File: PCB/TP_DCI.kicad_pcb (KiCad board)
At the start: 2 copper layers, 85.7 x 178.9 mm, 70 parts, among them J8 Molex_KK254, J9 Molex_KK254, K1 G5V-1, K2 G5V-1, P1 Conn_Poncho2P_2x_20x2, Q1 BC817W, Q2 BC817W, U1 PS2805-4, U2 ACS725xLCTR-10AU, U4 ACS725xLCTR-10AU, U5 24AA1025, U6 DS3231

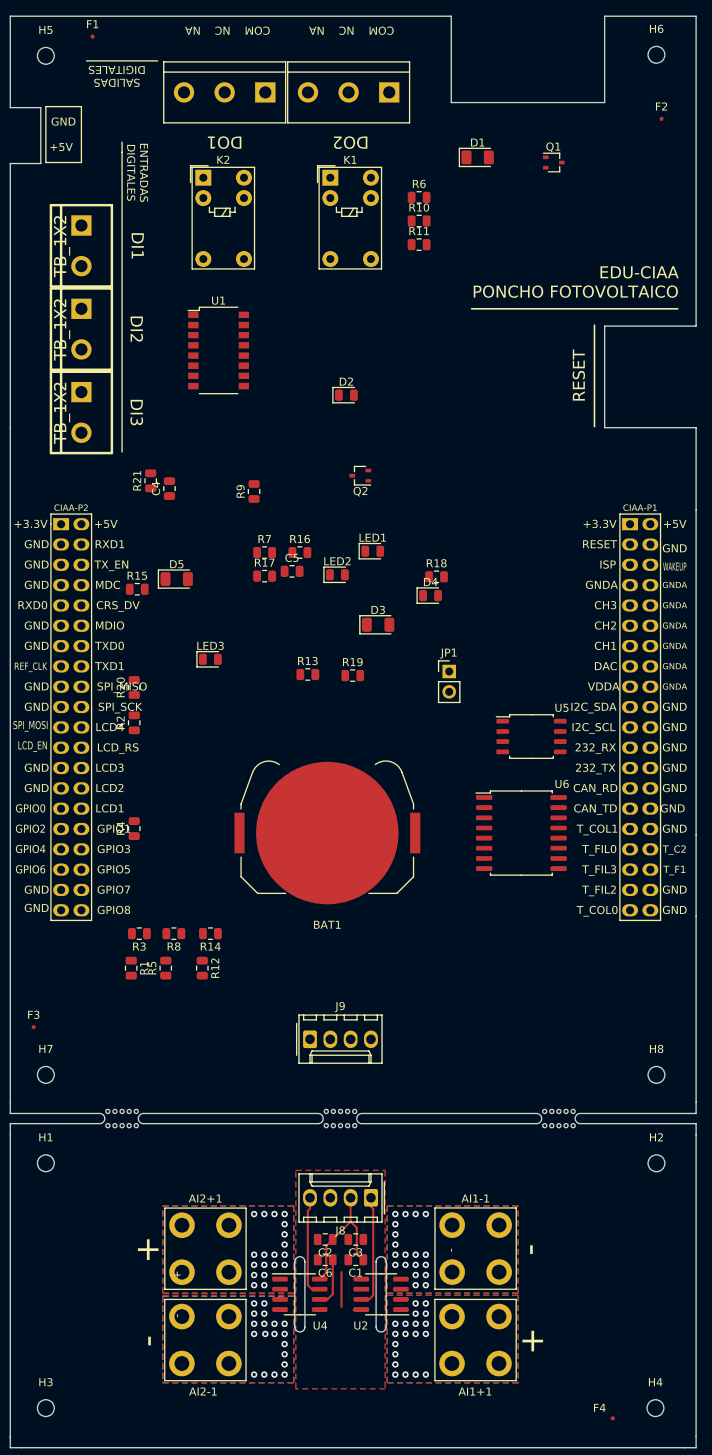
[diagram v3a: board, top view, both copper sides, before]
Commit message: actualizaciones de esquematico segun correcciones del docente
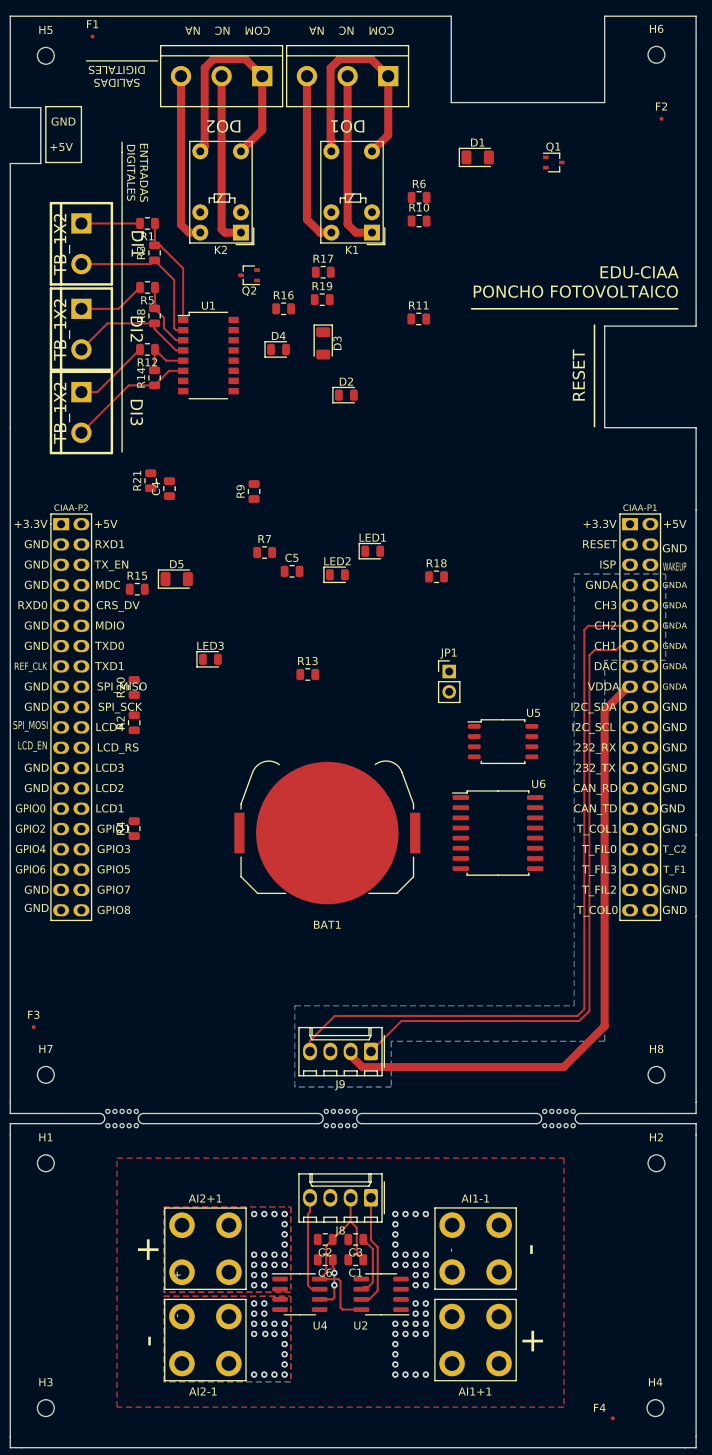
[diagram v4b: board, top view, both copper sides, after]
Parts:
- H1, H2, H3, H4: value Hole -> MountingHole
- moved R1 93.1 mm to (36.8, 43.8), turned to 180 degrees
- moved R5 85.1 mm to (36.8, 51.8), turned to 180 degrees
- moved R3 85.1 mm to (37.7, 47.5), turned to 90 degrees
- moved R12 77.6 mm to (36.8, 59.6), turned to 180 degrees
- moved R8 77.3 mm to (37.7, 55.4), turned to 90 degrees
- moved R14 69.8 mm to (37.7, 63.1), turned to 90 degrees
- moved R19 47.1 mm to (58.7, 53.3)
- moved R17 38.7 mm to (58.8, 49.9)
- moved D4 36.2 mm to (53.2, 59.6)
- moved D3 35.8 mm to (58.8, 58.8), turned to 270 degrees
- moved R16 30.5 mm to (53.8, 54.5)
- moved Q2 28.7 mm to (49.5, 50.3)
- moved DO2 16.0 mm to (46.1, 25.4)
- moved DO1 15.5 mm to (61.8, 25.4)
- moved R11 9.29 mm to (70.7, 55.8)
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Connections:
- P1 pad 10: (no net) -> GNDA
- P1 pad 7: (no net) -> GNDA
- P1 pad 8: (no net) -> GNDA
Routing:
- net /ADC_CH2: track 0.00 -> 90.6 mm
- net /ADC_CH1: track 0.00 -> 79.4 mm
- net VDDA: track 0.00 -> 78.8 mm
- net /COM2: track 0.00 -> 29.7 mm
- net /COM1: track 0.00 -> 29.2 mm
- net /NC1: track 0.00 -> 22.0 mm
- net /NC2: track 0.00 -> 21.7 mm
- net /NA1: track 0.00 -> 21.6 mm
- net /NA2: track 0.00 -> 21.4 mm
- net Net-(DI1-Pad2): track 0.00 -> 20.1 mm
- net Net-(DI2-Pad2): track 0.00 -> 16.1 mm
- net Net-(DI3-Pad2): track 0.00 -> 15.9 mm
- net Net-(R1-Pad1): track 0.00 -> 14.0 mm
- net Net-(DI3-Pad1): track 0.00 -> 9.53 mm
- net Net-(R5-Pad1): track 0.00 -> 8.63 mm
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- added copper zone on B.Cu, net GNDA
- removed copper zone on B.Cu, net Net-(AI1+1-Pad1)
- removed copper zone on F.Cu, net Net-(AI1+1-Pad1)
- removed copper zone on B.Cu, net Net-(AI1-1-Pad1)
- removed copper zone on F.Cu, net Net-(AI1-1-Pad1)
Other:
- outline, holes or cut-outs redrawn
- net class Default: clearance 0.2 -> 0.35
- rule trace_clearance: 0.2 -> 0.35

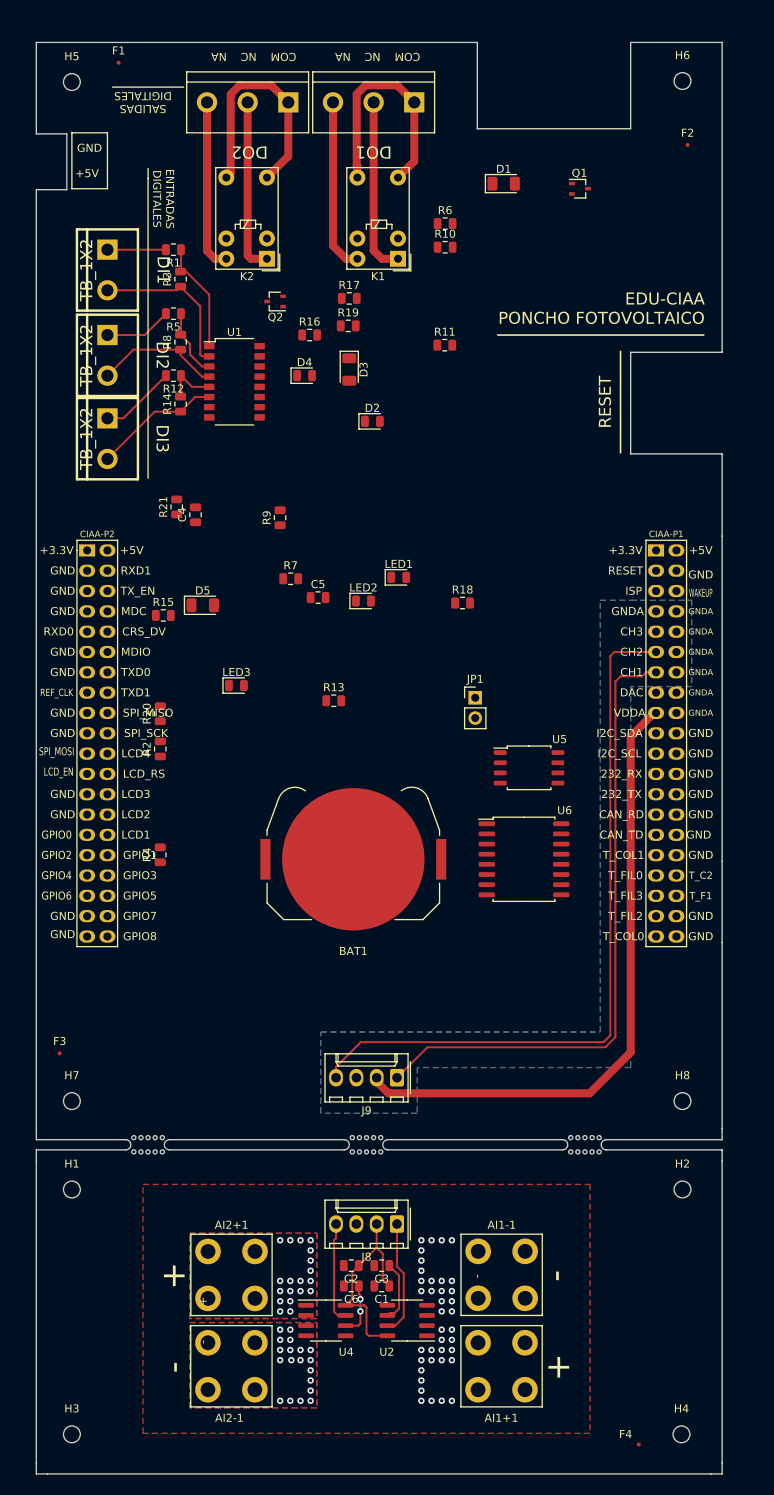
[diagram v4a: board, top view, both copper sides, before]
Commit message: avances en ruteo del PCB
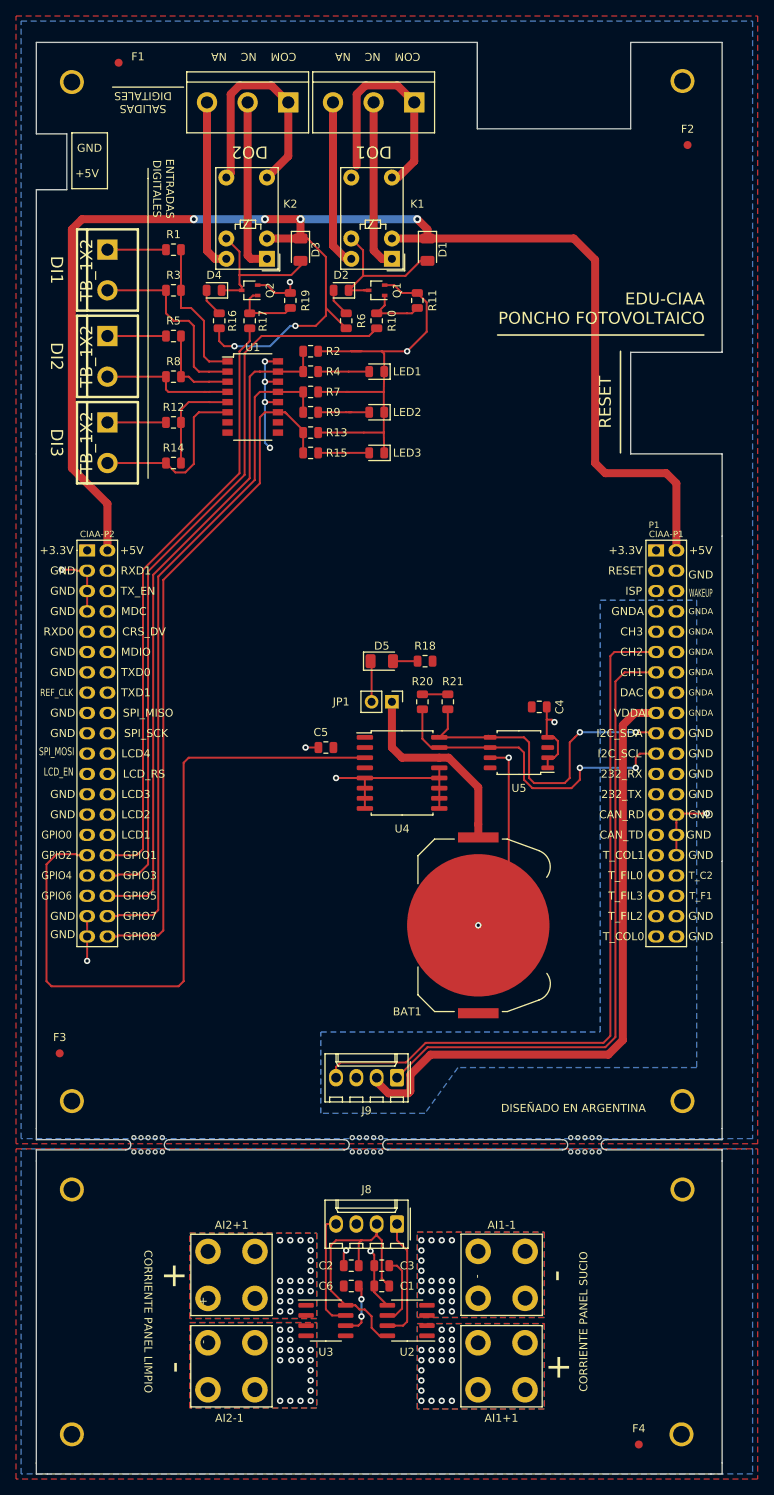
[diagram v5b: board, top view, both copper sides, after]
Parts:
- F1, F2, F3, F4: footprint Fiducial:Fiducial_0.5mm_Mask1mm -> Fiducial:Fiducial_1mm_Mask2mm
- moved R4 63.3 mm to (54.0, 59.1), turned to 0 degrees
- moved R2 53.2 mm to (54.0, 56.5), turned to 0 degrees
- moved C4 49.2 mm to (82.5, 101.0), turned to 0 degrees
- moved R21 41.7 mm to (71.1, 100.3), turned to 270 degrees
- moved LED3 34.0 mm to (62.2, 69.2), turned to 180 degrees
- moved R13 33.6 mm to (54.0, 66.7)
- moved R20 32.8 mm to (67.9, 100.3), turned to 270 degrees
- moved Q1 28.4 mm to (62.2, 48.9), turned to 180 degrees
- moved R15 27.4 mm to (54.0, 69.2)
- moved LED1 25.9 mm to (62.2, 59.1), turned to 180 degrees
- moved LED2 23.7 mm to (62.2, 64.1), turned to 180 degrees
- moved R7 23.5 mm to (54.0, 61.6)
- moved D5 23.4 mm to (62.9, 95.2)
- moved C5 18.8 mm to (55.9, 106.0), turned to 180 degrees
- moved U4 18.7 mm to (65.4, 109.2)
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- renumbered U4 to U3, U6 to U4
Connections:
- C4 pad 1: /+3.3V -> +3V3
- C5 pad 1: /+3.3V -> +3V3
- P1 pad 72: /GPIO1 -> Net-(P1-Pad72)
- P1 pad 74: /GPIO3 -> Net-(P1-Pad74)
- P1 pad 76: /GPIO5 -> Net-(P1-Pad76)
- P1 pad 78: /GPIO7 -> Net-(P1-Pad78)
- P1 pad 80: /GPIO8 -> Net-(P1-Pad80)
- R10 pad 2: /GPIO7 -> Net-(P1-Pad74)
- R13 pad 1: /GPIO5 -> Net-(P1-Pad80)
- R14 pad 1: Net-(DI3-Pad2) -> Net-(R12-Pad1)
- R14 pad 2: Net-(R12-Pad1) -> Net-(DI3-Pad2)
- R15 pad 1: /GPIO5 -> Net-(P1-Pad80)
- R17 pad 2: /GPIO8 -> Net-(P1-Pad72)
- R2 pad 1: /GPIO1 -> Net-(P1-Pad76)
- R3 pad 1: Net-(DI1-Pad2) -> Net-(R1-Pad1)
- R3 pad 2: Net-(R1-Pad1) -> Net-(DI1-Pad2)
- R4 pad 1: /GPIO1 -> Net-(P1-Pad76)
- R7 pad 1: /GPIO3 -> Net-(P1-Pad78)
- R8 pad 1: Net-(DI2-Pad2) -> Net-(R5-Pad1)
- R8 pad 2: Net-(R5-Pad1) -> Net-(DI2-Pad2)
- R9 pad 1: /GPIO3 -> Net-(P1-Pad78)
- U1 pad 11: /GPIO5 -> Net-(P1-Pad80)
- U1 pad 13: /GPIO3 -> Net-(P1-Pad78)
- U1 pad 15: /GPIO1 -> Net-(P1-Pad76)
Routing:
- net +5V: track 0.00 -> 198.6 mm, vias 0 -> 6
- net GND: track 0.00 -> 142.9 mm, vias 0 -> 10
- net Net-(P1-Pad74): track 0.00 -> 92.4 mm
- net /GPIO2: track 0.00 -> 88.2 mm
- net Net-(P1-Pad80): track 0.00 -> 86.2 mm
- net Net-(P1-Pad76): track 0.00 -> 84.8 mm
- net Net-(P1-Pad78): track 0.00 -> 84.7 mm
- net Net-(P1-Pad72): track 0.00 -> 75.4 mm
- net /SDA: track 0.00 -> 41.9 mm, vias 0 -> 2
- net /SCL: track 0.00 -> 40.8 mm, vias 0 -> 2
- net Net-(BAT1-Pad1): track 0.00 -> 24.8 mm
- net Net-(D1-Pad2): track 0.00 -> 19.8 mm
- net +3V3: track 0.00 -> 19.7 mm, vias 0 -> 4
- net Net-(D3-Pad2): track 0.00 -> 18.5 mm
- net Net-(C1-Pad2): track 0.00 -> 9.69 mm, vias 0 -> 2
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- added copper zone on F.Cu, net +3V3
- added copper zone on B.Cu, net GND
- added copper zone on B.Cu, net Net-(AI1+1-Pad1)
- added copper zone on F.Cu, net Net-(AI1+1-Pad1)
- added copper zone on B.Cu, net Net-(AI1-1-Pad1)
- added copper zone on F.Cu, net Net-(AI1-1-Pad1)
- added copper zone on B.Cu, net Net-(C1-Pad2)
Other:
- net class Default: clearance 0.35 -> 0.3
- rule trace_clearance: 0.35 -> 0.3
- board text added: "CORRIENTE PANEL LIMPIO"
- board text added: "CORRIENTE PANEL SUCIO"
- board text added: "DISEÑADO EN ARGENTINA"
